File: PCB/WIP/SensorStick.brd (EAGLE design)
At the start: 69.8 x 72.1 mm, 93 parts, among them U1 TPD4F003DQDR, U10 LIS3MDLTR, U11 LIS3MDLTR, U2 BMI088, U3 BMI088, U4 BMI088, U5 STM32H743ZIT6, U9 LIS3MDLTR, Y1 ECS-TXO-3225MV-400-TR

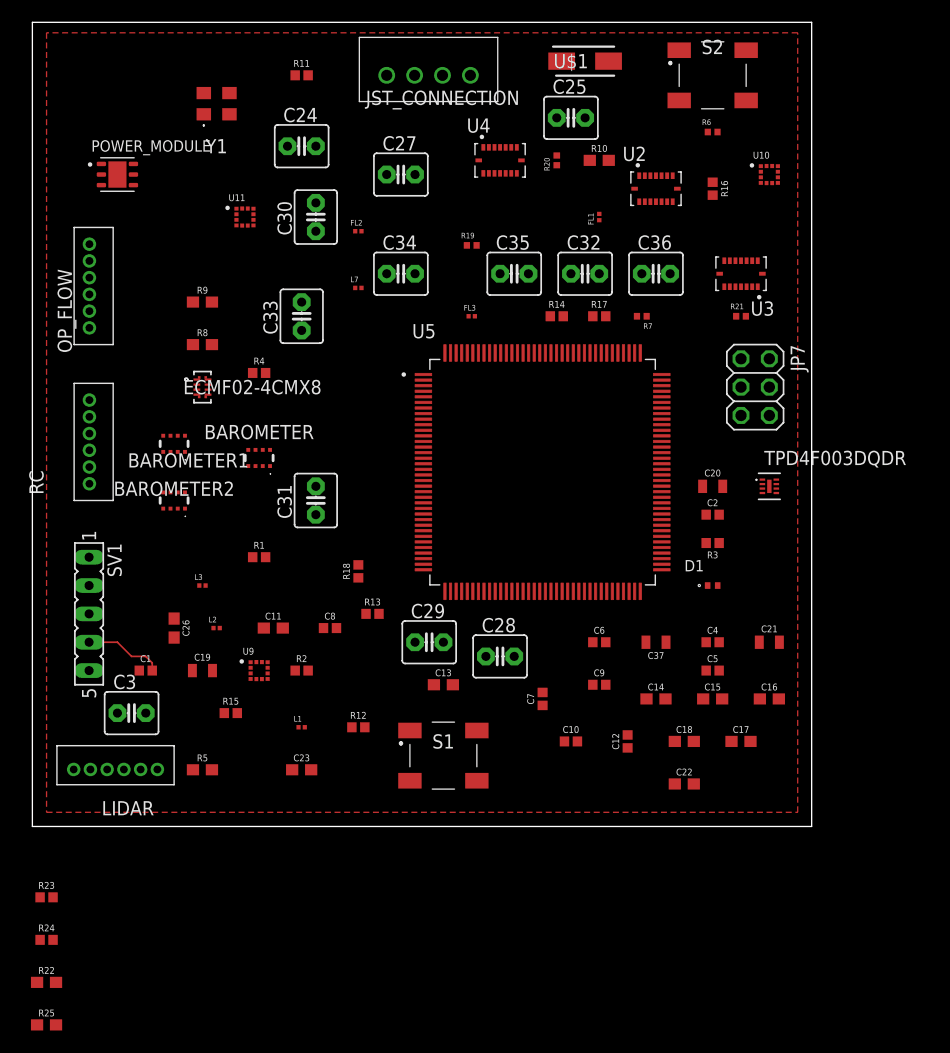
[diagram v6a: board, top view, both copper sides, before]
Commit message: rearranged everything again and grouped relevant components together, still a lot of clearance errors when wiring
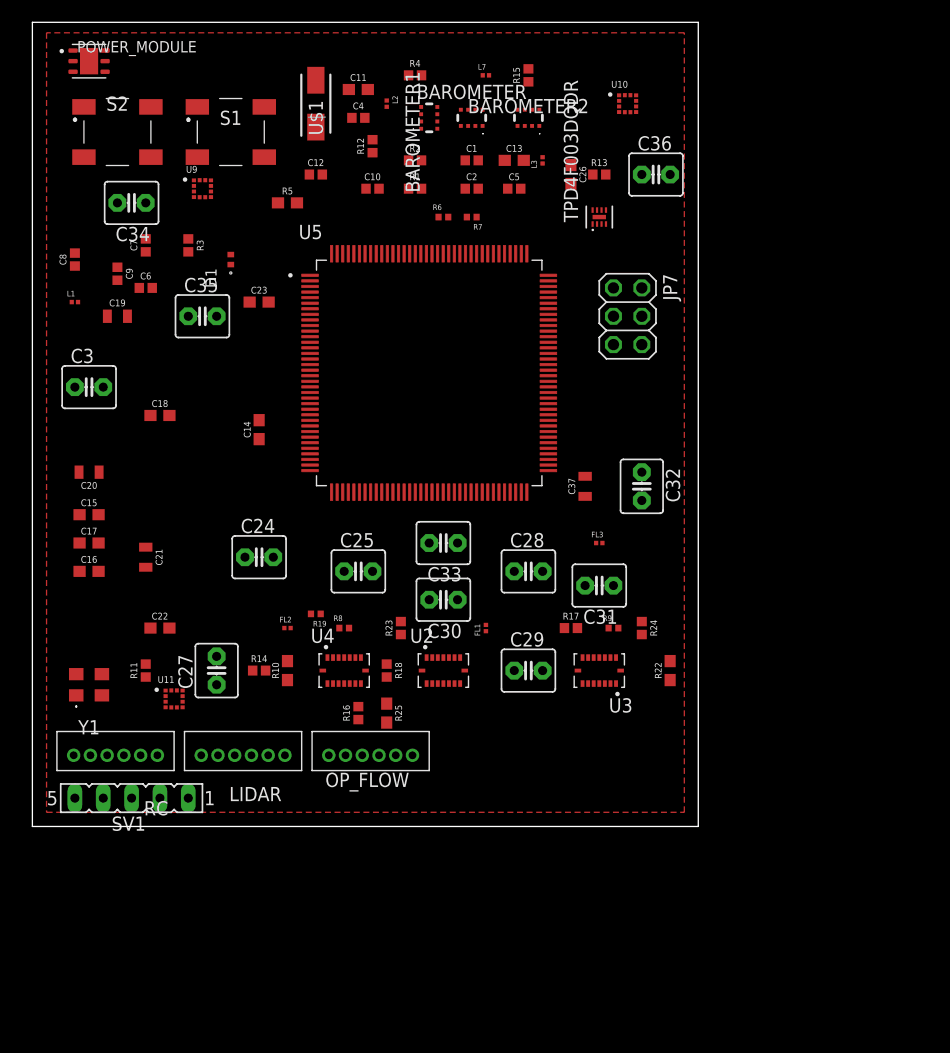
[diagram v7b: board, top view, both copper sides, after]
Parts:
- removed JST_CONNECTION: B4B-XH-A_LF__SN_, B4B-XH-A_LF__SN_:B4BXHALFSN
- removed R20, R21: RT0402FRE07220RL, ce-capstone:RESC1005X35N
- removed USB_COMM_MODE_FILTER: ECMF02-4CMX8, ECMF02-4CMX8:MICRO_QFN-8L_STM
- R8, R9: value 4.7k -> RT0402FRE07220RL; device SparkFun-Resistors:0603 -> ce-capstone:RESC1005X35N
- moved R15 63.1 mm to (53.3, 67.3), turned to 90 degrees
- moved R22 62.5 mm to (66.0, 14.0), turned to 90 degrees
- moved C16 62.0 mm to (14.0, 22.9)
- moved C17 61.1 mm to (14.0, 25.4)
- moved R24 60.2 mm to (63.5, 17.8), turned to 270 degrees
- moved S1 59.0 mm to (26.7, 62.2)
- moved C15 58.3 mm to (14.0, 27.9)
- moved C12 58.0 mm to (34.3, 58.4), turned to 0 degrees
- moved C9 56.8 mm to (16.5, 49.5), turned to 270 degrees
- moved C4 56.7 mm to (38.1, 63.5)
- moved R16 56.7 mm to (38.1, 10.2), turned to 90 degrees
- moved C21 56.4 mm to (19.1, 24.1), turned to 270 degrees
- moved C20 55.9 mm to (14.0, 31.8), turned to 180 degrees
- moved C18 55.3 mm to (20.3, 36.8)
- moved R11 55.1 mm to (19.1, 14.0), turned to 90 degrees
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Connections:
- net GPIO_EXTI0_1 renamed GPIO_EXTI00
- removed net DN: JST_CONNECTION.3, USB_COMM_MODE_FILTER.2
- removed net DP: JST_CONNECTION.2, USB_COMM_MODE_FILTER.3
- removed net EXTI1_1: R24.2, U2.12
- removed net GPIO_EXTI1_1: R24.1, U5.57
- removed net USB_DN: USB_COMM_MODE_FILTER.7
- removed net USB_DP: USB_COMM_MODE_FILTER.6
- net 3V3: no longer R8.2, R9.1, USB_COMM_MODE_FILTER.1
- net 5V_IN: no longer JST_CONNECTION.4
- net CSB_ACCEL2: now also R9.2; no longer R21.2
- net CSB_GYRO1: now also R8.2; no longer R20.2
- net EXTI0_1: now also U2.12; no longer U2.16
- net EXTI1: now also R24.2
- net EXTI4: now also U2.16
- net GND: no longer JST_CONNECTION.1, USB_COMM_MODE_FILTER.5, USB_COMM_MODE_FILTER.8
- net GPIO_EXTI1: now also R24.1
- net I2C1_SCL: no longer R8.1
- net I2C1_SDA: no longer R9.2
- net N$16: now also R8.1; no longer R20.1
- net N$17: now also R9.1; no longer R21.1
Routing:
- net GND: track 7.12 -> 0.00 mm
- net 3V3: track 1.27 -> 0.00 mm
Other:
- board size 69.8 x 72.1 mm -> 59.7 x 72.1 mm

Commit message: might keep this one, still a lot of airwires
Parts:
- moved R3 1.27 mm to (22.9, 53.3), turned to 0 degrees
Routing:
- net GND: track 0.00 -> 330.3 mm, vias 0 -> 1
- net SPI6_MISO: track 0.00 -> 110.9 mm, vias 0 -> 2
- net SPI6_MOSI: track 0.00 -> 106.5 mm, vias 0 -> 2
- net SPI6_SCK: track 0.00 -> 102.6 mm, vias 0 -> 2
- net GPIO_EXTI1: track 0.00 -> 99.4 mm, vias 0 -> 2
- net SPI6_CS: track 0.00 -> 86.8 mm, vias 0 -> 1
- net NRST: track 0.00 -> 79.1 mm, vias 0 -> 4
- net I2C4_SDA: track 0.00 -> 70.3 mm, vias 0 -> 2
- net 5V: track 0.00 -> 60.5 mm
- net N$7: track 0.00 -> 58.8 mm, vias 0 -> 1
- net UART5_TX: track 0.00 -> 58.5 mm, vias 0 -> 1
- net UART5_RX: track 0.00 -> 55.2 mm, vias 0 -> 1
- net GPIO_EXTI2: track 0.00 -> 51.7 mm, vias 0 -> 2
- net I2C4_SCL: track 0.00 -> 51.5 mm
- net CSB_GYRO2: track 0.00 -> 50.9 mm, vias 0 -> 2
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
